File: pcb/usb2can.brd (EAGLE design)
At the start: 59 x 15.8 mm, 49 parts, among them CON1 USB_A_MALESMD, IC1 ADM3053M, IC2 LD1117S33

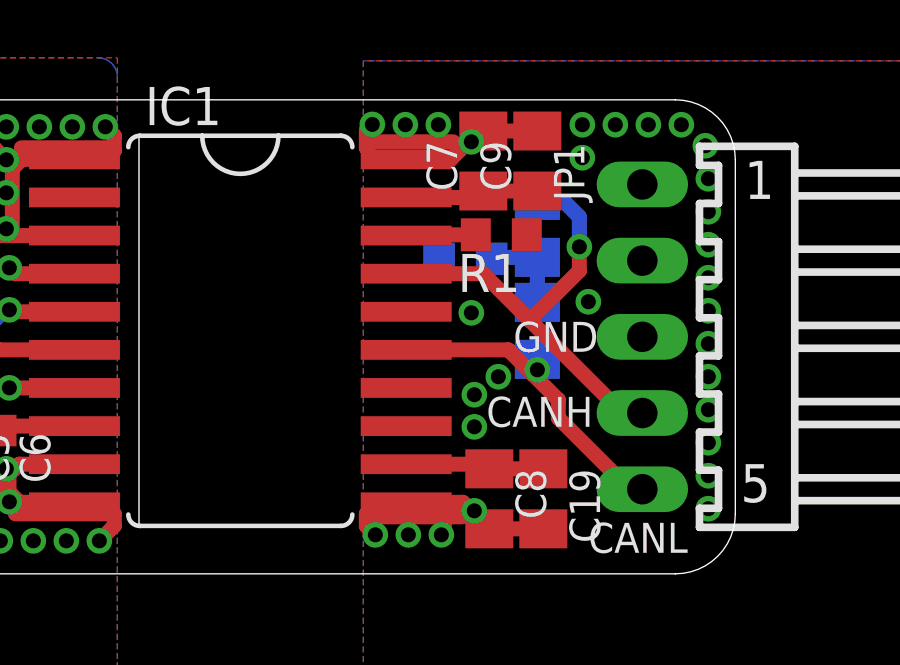
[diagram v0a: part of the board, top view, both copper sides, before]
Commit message: pcb: fix CAN transceiver V_ISOIN and V_ISOOUT not connected
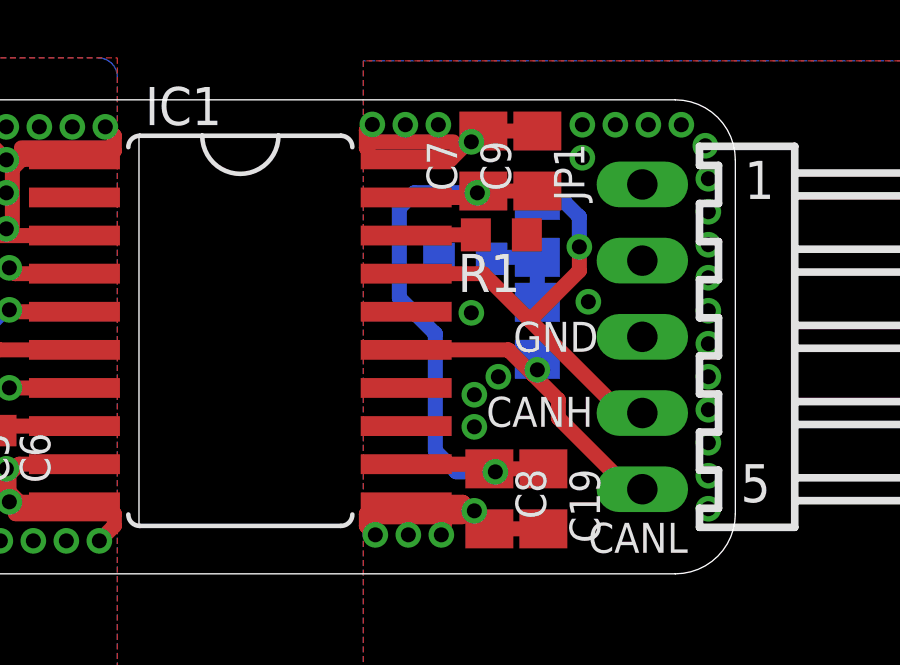
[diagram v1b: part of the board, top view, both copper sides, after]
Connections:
- removed net N$10: C7.1, C9.1, IC1.19
- net N$8: now also C7.1, C9.1, IC1.19
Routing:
- net N$8: track 4.72 -> 23.3 mm, vias 0 -> 2
- net N$10: track 4.45 -> 0.00 mm
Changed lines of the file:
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@@
 <layer number="14" name="Route14" color="1" fill="6" visible="no" active="no"/>
 <layer number="15" name="Route15" color="4" fill="6" visible="no" active="no"/>
-<layer number="16" name="Bottom" color="1" fill="1" visible="yes" active="yes"/>
+<layer number="16" name="Bottom" color="1" fill="1" visible="no" active="yes"/>
 <layer number="17" name="Pads" color="2" fill="1" visible="yes" active="yes"/>
 <layer number="18" name="Vias" color="2" fill="1" visible="yes" active="yes"/>
 <layer number="19" name="Unrouted" color="6" fill="1" visible="yes" active="yes"/>
 <layer number="20" name="Dimension" color="15" fill="1" visible="yes" active="yes"/>
-<layer number="21" name="tPlace" color="7" fill="1" visible="yes" active="yes"/>
-<layer number="22" name="bPlace" color="7" fill="1" visible="yes" active="yes"/>
+<layer number="21" name="tPlace" color="7" fill="1" visible="no" active="yes"/>
+<layer number="22" name="bPlace" color="7" fill="1" visible="no" active="yes"/>
 <layer number="23" name="tOrigins" color="15" fill="1" visible="yes" active="yes"/>
-<layer number="24" name="bOrigins" color="15" fill="1" visible="yes" active="yes"/>
+<layer number="24" name="bOrigins" color="15" fill="1" visible="no" active="yes"/>
 <layer number="25" name="tNames" color="7" fill="1" visible="no" active="yes"/>
 <layer number="26" name="bNames" color="7" fill="1" visible="no" active="yes"/>
@@
 <layer number="38" name="bTest" color="7" fill="1" visible="no" active="yes"/>
 <layer number="39" name="tKeepout" color="4" fill="11" visible="yes" active="yes"/>
-<layer number="40" name="bKeepout" color="1" fill="11" visible="yes" active="yes"/>
+<layer number="40" name="bKeepout" color="1" fill="11" visible="no" active="yes"/>
 <layer number="41" name="tRestrict" color="4" fill="10" visible="yes" active="yes"/>
-<layer number="42" name="bRestrict" color="1" fill="10" visible="yes" active="yes"/>
+<layer number="42" name="bRestrict" color="1" fill="10" visible="no" active="yes"/>
 <layer number="43" name="vRestrict" color="2" fill="10" visible="yes" active="yes"/>
 <layer number="44" name="Drills" color="7" fill="1" visible="no" active="yes"/>
@@
 <layer number="50" name="dxf" color="7" fill="1" visible="no" active="no"/>
 <layer number="51" name="tDocu" color="7" fill="1" visible="yes" active="yes"/>
-<layer number="52" name="bDocu" color="7" fill="1" visible="yes" active="yes"/>
+<layer number="52" name="bDocu" color="7" fill="1" visible="no" active="yes"/>
 <layer number="53" name="tGND_GNDA" color="7" fill="9" visible="no" active="no"/>
 <layer number="54" name="bGND_GNDA" color="1" fill="9" visible="no" active="no"/>
@@
 <contactref element="C8" pad="1"/>
 <contactref element="IC1" pad="12"/>
-<wire x1="50.545" y1="3.755" x2="50.8" y2="3.5" width="0.5" layer="1"/>
 <wire x1="50.8" y1="3.5" x2="52.6" y2="3.5" width="0.5" layer="1"/>
 <wire x1="50.545" y1="3.755" x2="50.445" y2="3.655" width="0.5" layer="1"/>
 <wire x1="50.445" y1="3.655" x2="48.0292" y2="3.655" width="0.5" layer="1"/>
-</signal>
-<signal name="N$10">
 <contactref element="C7" pad="1"/>
 <contactref element="C9" pad="1"/>
@@
 <wire x1="50.6" y1="12.76" x2="50.345" y2="12.545" width="0.5" layer="1"/>
 <wire x1="50.345" y1="12.545" x2="48.0292" y2="12.545" width="0.5" layer="1"/>
+<wire x1="50.345" y1="12.545" x2="50.4" y2="12.545" width="0.5" layer="1"/>
+<wire x1="50.4" y1="12.545" x2="50.4" y2="12.7" width="0.5" layer="1"/>
+<via x="50.4" y="12.7" extent="1-16" drill="0.5"/>
+<wire x1="50.4" y1="12.7" x2="48.3" y2="12.7" width="0.5" layer="16"/>
+<wire x1="48.3" y1="12.7" x2="47.8" y2="12.2" width="0.5" layer="16"/>
+<wire x1="50.545" y1="3.755" x2="50.8" y2="3.5" width="0.5" layer="1"/>
+<wire x1="50.8" y1="3.5" x2="50.9" y2="3.5" width="0.5" layer="1"/>
+<wire x1="50.9" y1="3.5" x2="51" y2="3.4" width="0.5" layer="1"/>
+<via x="51" y="3.4" extent="1-16" drill="0.5"/>
+<wire x1="47.8" y1="12.2" x2="47.8" y2="9.2" width="0.5" layer="16"/>
+<wire x1="47.8" y1="9.2" x2="49" y2="8" width="0.5" layer="16"/>
+<wire x1="49" y1="8" x2="49" y2="4.1" width="0.5" layer="16"/>
+<wire x1="49" y1="4.1" x2="49.7" y2="3.4" width="0.5" layer="16"/>
+<wire x1="51" y1="3.4" x2="49.7" y2="3.4" width="0.5" layer="16"/>
 </signal>
 <signal name="N$9">

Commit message: pcb: adapt resistor values for LEDs
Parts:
- R10: value 330R -> 270R
- R7, R9: value 33R -> 120R
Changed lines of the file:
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@@
 <element name="C19" library="rcl" package="C0805K" value="100n" x="52.6" y="2.5" rot="R270"/>
 <element name="LED2" library="led" package="CHIPLED_0603" value="BLUE" x="29.9" y="4.3" rot="R90"/>
-<element name="R7" library="resistor" package="R0603" value="33R" x="23.9" y="12.1" rot="MR180"/>
+<element name="R7" library="resistor" package="R0603" value="120R" x="23.9" y="12.1" rot="MR180"/>
 <element name="S3" library="micro_switch" package="MICRO_SWITCH_3X6X2.5" value="MICRO_SWITCH_3X6X2.5S" x="29.4" y="10.858575" rot="R270"/>
 <element name="LED3" library="led" package="CHIPLED_0603" value="RED" x="27.3" y="2.8" rot="R90"/>
 <element name="R8" library="resistor" package="R0603" value="330R" x="23.9" y="10.3" rot="MR180"/>
 <element name="LED4" library="led" package="CHIPLED_0603" value="WHITE" x="29.9" y="5.4" rot="R90"/>
-<element name="R9" library="resistor" package="R0603" value="33R" x="23.9" y="13.9" rot="MR180"/>
+<element name="R9" library="resistor" package="R0603" value="120R" x="23.9" y="13.9" rot="MR180"/>
 <element name="LED5" library="led" package="CHIPLED_0603" value="GREEN" x="27.3" y="1.7" rot="R90"/>
-<element name="R10" library="resistor" package="R0603" value="330R" x="24.6" y="1.75"/>
+<element name="R10" library="resistor" package="R0603" value="270R" x="24.6" y="1.75"/>
 <element name="TP3" library="testpad" package="TP07R" value="TPSTP07R" x="23.08" y="3.62">
 <attribute name="TP_SIGNAL_NAME" value="" x="23.08" y="3.62" size="1.778" layer="27" display="off"/>
